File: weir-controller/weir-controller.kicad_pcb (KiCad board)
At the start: 2 copper layers, 93 x 65 mm, 40 parts, among them J1 Screw_Terminal_01x02, J2 Screw_Terminal_01x04, J3 Screw_Terminal_01x04, J4 USB_B_Mini, J5 Wurth_74980104400, J6 Screw_Terminal_01x02, Q1 PSMN0R7-25YLD, Q2 PSMN0R7-25YLD, Q3 PSMN0R7-25YLD, Q4 PSMN0R7-25YLD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

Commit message: Fix a bunch of fuck ups
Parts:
- added D1: LED_ABGR, LED_SMD:LED_Cree-PLCC4_2x2mm_CW, F.Cu at (146.2, 52.1)
- added G***: LOGO, custom-parts:1_1_0_version_tag, F.Cu at (159.3, 63.5)
- added G***: LOGO, custom-parts:weir_controller_text, F.Cu at (109.1, 43.9)
- added R13: 80, Resistor_SMD:R_0805_2012Metric_Pad1.15x1.40mm_HandSolder, F.Cu at (146.2, 49.6)
- added SW1: SW_Push, custom-parts:PTS636, F.Cu at (114.8, 56.4)
- J6: footprint custom-parts:PhoenixContact_PTSA_2Pin -> custom-parts:PhoenixContact_PTSA_2PIN_8A
- U2: footprint Package_DFN_QFN:WQFN-24-1EP_4x4mm_P0.5mm_EP2.6x2.6mm_ThermalVias -> custom-parts:TI_RMQ0024A
- moved R5 3.85 mm to (153.3, 71.3), turned to 315 degrees
- moved C12 3.26 mm to (80.6, 76.1)
- moved C11 2.82 mm to (76.7, 76.1), turned to 0 degrees
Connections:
- net Net-(J1-Pad2) renamed /RELAY_NEGATIVE
- net Net-(J2-Pad1) renamed /RED_CATHODE
- net Net-(J2-Pad2) renamed /GREEN_CATHODE
- net Net-(J2-Pad3) renamed /BLUE_CATHODE
- U1 pad 13: Net-(U1-Pad13) -> /IND_R
- U1 pad 24: Net-(U1-Pad24) -> /RELAY_ON_G
- U1 pad 26: Net-(U1-Pad26) -> /RED_G
- U1 pad 30: Net-(U1-Pad30) -> /IND_G
- U1 pad 37: Net-(U1-Pad37) -> /IND_B
- U1 pad 6: /RELAY_ON_G -> Net-(U1-Pad6)
- U1 pad 7: /RED_G -> /FACTORY_RESET
- U4 pad 1: GND -> +12V
- U4 pad 2: +3V3 -> GND
- U4 pad 3: +12V -> +3V3
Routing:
- net /IND_R: track 0.00 -> 35.1 mm, vias 0 -> 2
- net /IND_G: track 0.00 -> 21.3 mm, vias 0 -> 2
- net /RELAY_ON_G: track 41.9 -> 61.6 mm
- net /RED_G: track 34.1 -> 53.8 mm, vias 2 -> 4
- net +3V3: track 163.3 -> 178.5 mm
- net /IND_B: track 0.00 -> 6.64 mm
- net /GREEN_CATHODE: track 26.6 -> 31.8 mm
- net /RELAY_NEGATIVE: track 15.1 -> 20.1 mm
- net /FACTORY_RESET: track 0.00 -> 4.93 mm
- net /RED_CATHODE: track 35.3 -> 30.4 mm
- net GND: track 12.4 -> 16.8 mm, vias 86 -> 108
- net /BLUE_CATHODE: track 35.2 -> 31.0 mm
- net Net-(R5-Pad1): track 5.64 -> 2.58 mm, vias 2 -> 0
- net /TX_D1: track 30.2 -> 28.1 mm, vias 4 -> 2
- net Net-(D1-Pad4): track 0.00 -> 2.06 mm
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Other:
- board text added: "Reset"
- board text removed: "Weir Controller"
- board text removed: "v1.0"

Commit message: v1.1.1
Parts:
- removed the G*** at (159.3, 63.5)
- removed the G*** at (109.1, 43.9)
- removed the REF** at (157.6, 45.6)
- removed the REF** at (75.8, 45.6)
- added G***: LOGO, custom-parts:v1.1.1_text, F.Cu at (94.1, 51.5)
- added G***: LOGO, custom-parts:weir_name_text, F.Cu at (99.8, 47.9)
- added R14: 33, Resistor_SMD:R_0805_2012Metric_Pad1.15x1.40mm_HandSolder, F.Cu at (142.7, 54.0)
- added R15: 33, Resistor_SMD:R_0805_2012Metric_Pad1.15x1.40mm_HandSolder, F.Cu at (142.7, 56.0)
- added R16: 33, Resistor_SMD:R_0805_2012Metric_Pad1.15x1.40mm_HandSolder, F.Cu at (142.7, 57.9)
- added R17: 33, Resistor_SMD:R_0805_2012Metric_Pad1.15x1.40mm_HandSolder, F.Cu at (147.4, 73.4)
- added R18: 33, Resistor_SMD:R_0805_2012Metric_Pad1.15x1.40mm_HandSolder, F.Cu at (148.8, 72.0)
- added R19: 33, Resistor_SMD:R_0805_2012Metric_Pad1.15x1.40mm_HandSolder, F.Cu at (146.1, 74.8)
- added R20: 33, Resistor_SMD:R_0805_2012Metric_Pad1.15x1.40mm_HandSolder, F.Cu at (142.7, 62.3)
- added REF**: 4MM_Mounting_Hole, custom-parts:4MM_Mounting_Hole, F.Cu at (157.6, 50.4)
- added REF**: 4MM_Mounting_Hole, custom-parts:4MM_Mounting_Hole, F.Cu at (75.6, 50.4)
- U1: footprint RF_Module:ESP32-WROOM-32U -> custom-parts:ESP32-WROOM-32U
- moved R6 10.0 mm to (150.2, 74.7), turned to 45 degrees
- moved U2 5.30 mm to (150.2, 78.5)
- moved C3 4.08 mm to (145.2, 81.4), turned to 225 degrees
- moved R5 3.76 mm to (154.2, 75.0), turned to 0 degrees
- moved C4 2.71 mm to (143.8, 80.0), turned to 225 degrees
- moved D1 2.36 mm to (145.4, 49.9)
- moved R13 2.36 mm to (145.4, 47.4)
- moved C6 1.81 mm to (140.9, 77.1), turned to 225 degrees
- moved C5 1.70 mm to (142.4, 78.5), turned to 225 degrees
- moved C7 1.41 mm to (161.8, 87.3)
- moved C9 1.41 mm to (159.8, 87.3)
- moved R8 1.41 mm to (140.6, 97.3)
- moved J5 1.41 mm to (150.4, 93.8)
- moved R7 1.41 mm to (160.2, 97.3)
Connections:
- J4 pad 4: Net-(J4-Pad4) -> (no net)
- R6 pad 2: /RX_D1 -> /RX_D1_M
- U1 pad 14: /PHY_INTR -> (no net)
- U1 pad 28: /PHY_50MHzIn -> Net-(R20-Pad2)
- U1 pad 31: /TX_D0 -> Net-(R16-Pad1)
- U1 pad 32: Net-(U1-Pad32) -> (no net)
- U1 pad 33: /TX_EN -> Net-(R15-Pad1)
- U1 pad 36: /TX_D1 -> Net-(R14-Pad2)
- U1 pad 4: Net-(U1-Pad4) -> (no net)
- U1 pad 5: Net-(U1-Pad5) -> (no net)
- U1 pad 6: Net-(U1-Pad6) -> (no net)
- U2 pad 12: Net-(U2-Pad12) -> (no net)
- U2 pad 17: /RX_D1 -> /RX_D1_M
- U2 pad 18: /RX_D0 -> Net-(R17-Pad2)
- U2 pad 20: /CRS_DV -> Net-(R19-Pad1)
- U2 pad 3: /PHY_INTR -> (no net)
- U3 pad 1: Net-(U3-Pad1) -> (no net)
- U3 pad 10: Net-(U3-Pad10) -> (no net)
- U3 pad 11: Net-(U3-Pad11) -> (no net)
- U3 pad 12: Net-(U3-Pad12) -> (no net)
- U3 pad 13: Net-(U3-Pad13) -> (no net)
- U3 pad 14: Net-(U3-Pad14) -> (no net)
- U3 pad 15: Net-(U3-Pad15) -> (no net)
- U3 pad 16: Net-(U3-Pad16) -> (no net)
- U3 pad 17: Net-(U3-Pad17) -> (no net)
- U3 pad 18: Net-(U3-Pad18) -> (no net)
- U3 pad 22: Net-(U3-Pad22) -> (no net)
- U3 pad 24: Net-(U3-Pad24) -> (no net)
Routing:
- net GND: track 16.8 -> 107.7 mm, vias 108 -> 125
- net +3V3: track 178.5 -> 215.3 mm, vias 5 -> 13
- net /PHY_INTR: track 33.1 -> 0.00 mm, vias 2 -> 0
- net /RX_D1: track 49.7 -> 38.3 mm, vias 2 -> 0
- net /MDIO: track 17.0 -> 27.8 mm
- net /RX_ER: track 26.8 -> 36.8 mm, vias 2 -> 0
- net /LED2: track 35.0 -> 25.9 mm
- net /LED0: track 38.9 -> 31.5 mm
- net /RD_P: track 12.8 -> 5.61 mm
- net /MDC: track 19.2 -> 25.8 mm
- net /TD_P: track 12.9 -> 7.25 mm
- net /RX_D0: track 44.3 -> 38.8 mm
- net /RX_D1_M: track 0.00 -> 4.63 mm
- net /PHY_50MHzIn: track 21.2 -> 25.6 mm
- net Net-(R17-Pad2): track 0.00 -> 4.21 mm
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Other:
- board size 93 x 65 mm -> 93 x 60.1 mm

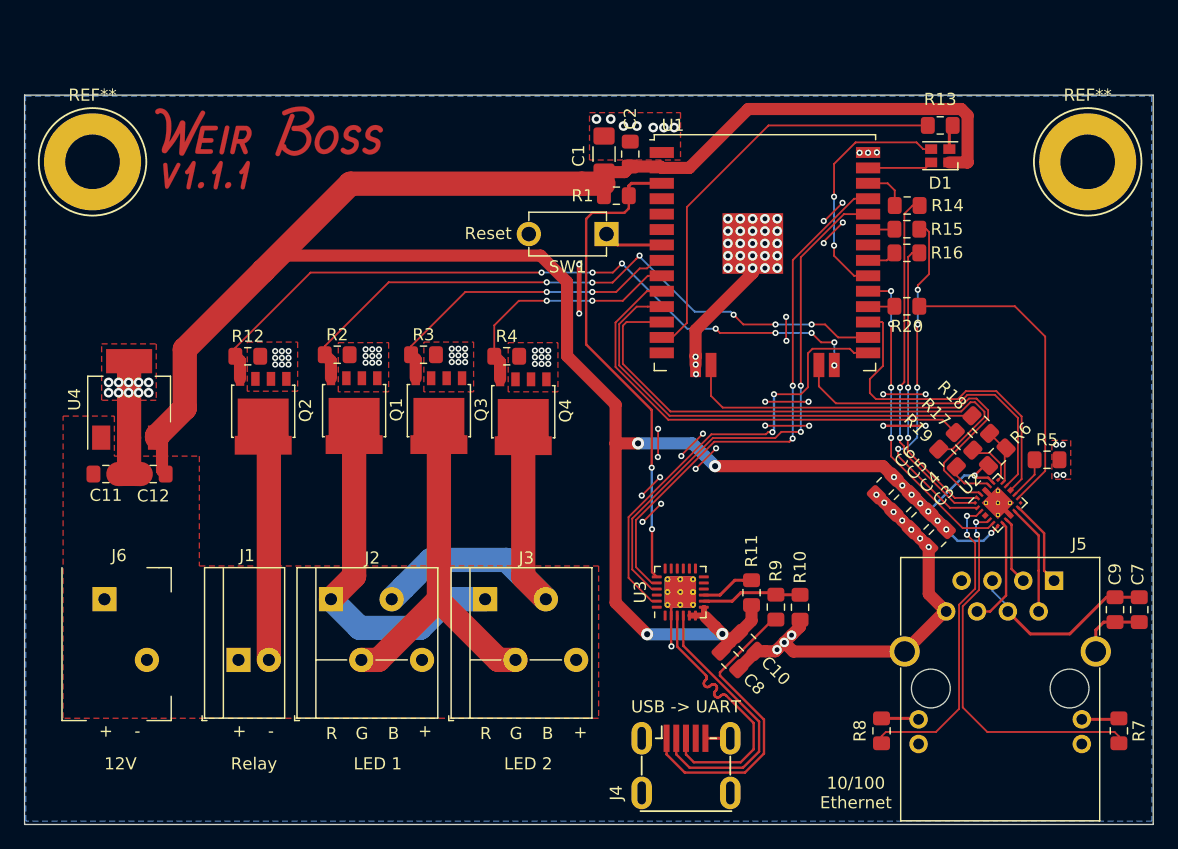
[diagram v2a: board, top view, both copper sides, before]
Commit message: Try 4 layer for RMII trace impedance
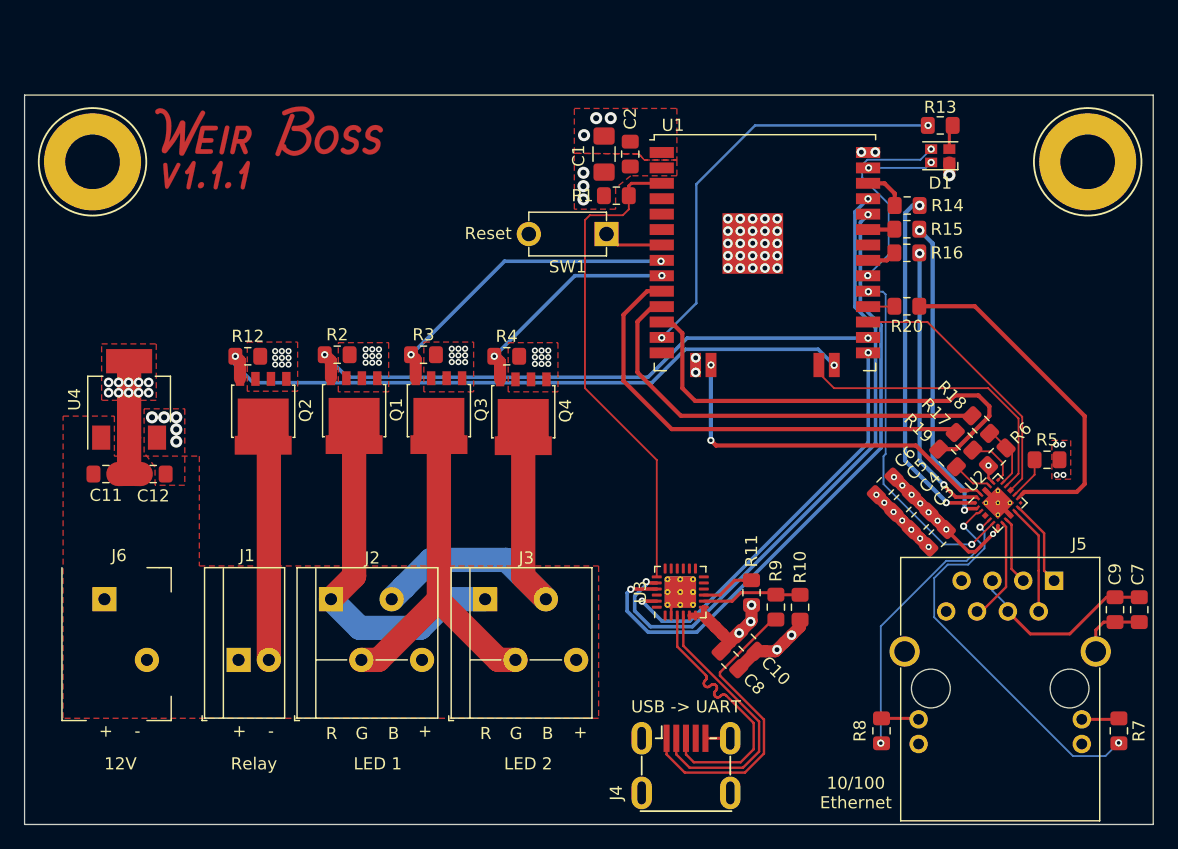
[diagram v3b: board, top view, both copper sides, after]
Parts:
- J4: footprint custom-parts:54819-0589 -> Custom:54819-0589
- J5: footprint custom-parts:Wurth_74980104400 -> Custom:Wurth_74980104400
- SW1: footprint custom-parts:PTS636 -> Custom:PTS636
- U1: footprint custom-parts:ESP32-WROOM-32U -> Custom:ESP32-WROOM-32U
- U2: footprint custom-parts:TI_RMQ0024A -> Custom:TI_RMQ0024A
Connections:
- REF** pad 1: (no net) -> GND (x2)
- U2 pad 12: (no net) -> Net-(U2-Pad12)
- U2 pad 3: (no net) -> Net-(U2-Pad3)
- U3 pad 1: (no net) -> Net-(U3-Pad1)
- U3 pad 10: (no net) -> Net-(U3-Pad10)
- U3 pad 11: (no net) -> Net-(U3-Pad11)
- U3 pad 12: (no net) -> Net-(U3-Pad12)
- U3 pad 13: (no net) -> Net-(U3-Pad13)
- U3 pad 14: (no net) -> Net-(U3-Pad14)
- U3 pad 15: (no net) -> Net-(U3-Pad15)
- U3 pad 16: (no net) -> Net-(U3-Pad16)
- U3 pad 17: (no net) -> Net-(U3-Pad17)
- U3 pad 18: (no net) -> Net-(U3-Pad18)
- U3 pad 22: (no net) -> Net-(U3-Pad22)
- U3 pad 24: (no net) -> Net-(U3-Pad24)
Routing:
- net +3V3: track 215.3 -> 31.8 mm, vias 13 -> 21
- net GND: track 107.7 -> 35.9 mm, vias 125 -> 91
- net /RX: track 45.1 -> 52.2 mm
- net /TX: track 44.8 -> 51.7 mm
- net /RX_ER: track 36.8 -> 30.3 mm, vias 0 -> 2
- net /MDIO: track 27.8 -> 22.4 mm
- net /RELAY_ON_G: track 59.6 -> 54.4 mm, vias 8 -> 2
- net /CRS_DV: track 43.8 -> 39.0 mm
- net /RED_G: track 53.6 -> 49.0 mm, vias 6 -> 2
- net /TX_EN: track 29.1 -> 25.6 mm, vias 4 -> 2
- net /PHY_50MHzIn: track 25.6 -> 28.9 mm
- net /BOOT_MODE: track 37.2 -> 34.0 mm
- net /IND_G: track 20.0 -> 17.0 mm
- net /RX_D1: track 38.3 -> 35.7 mm
- net /PHY_RST: track 26.5 -> 29.0 mm, vias 4 -> 2
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- added copper zone on F.Cu, net +3V3
- added copper zone on In1.Cu, net +3V3
- added copper zone on In2.Cu, net GND
- removed copper zone on B.Cu, net GND
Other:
- copper layers 2 -> 4
- rule trace_min: 0.1524 -> 0.127
